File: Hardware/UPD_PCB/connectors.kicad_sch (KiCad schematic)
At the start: 26 parts, among them J1 25A Fuse holder, J10 796739-2, J11 Conn_01x02, J12 Conn_01x01, J2 796739-2, J3 Conn_01x02, J4 1776119-2, J5 1776119-2, J6 1776119-2, J7 1776119-2, J8 1776119-2, J9 1776119-2

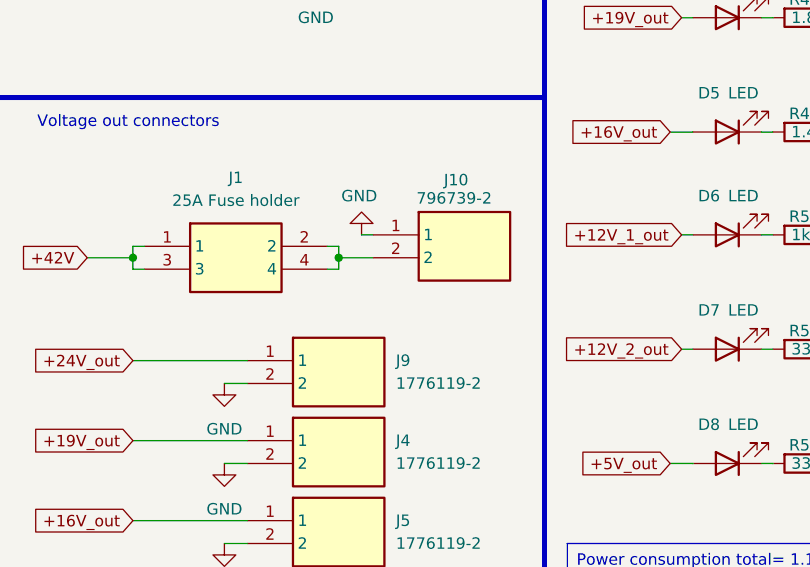
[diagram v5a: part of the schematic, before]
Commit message: Routed main traces
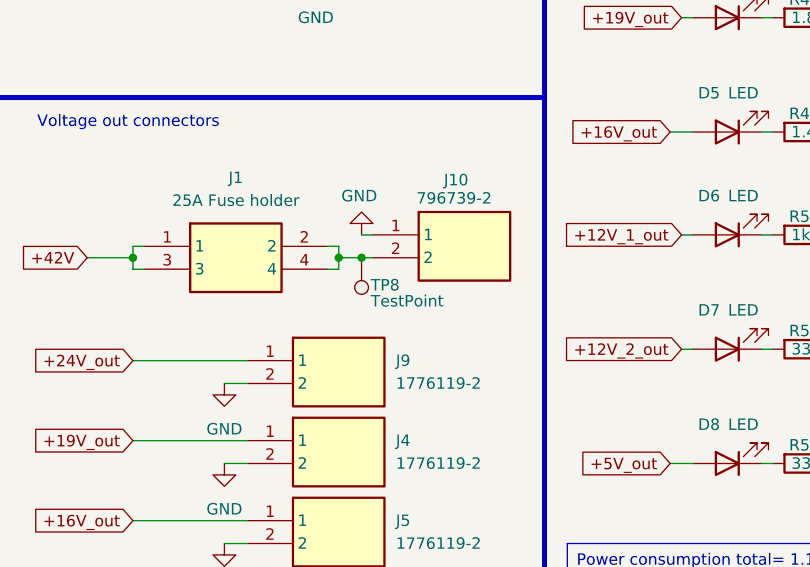
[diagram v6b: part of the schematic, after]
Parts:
- added TP8: TestPoint, TestPoint:TestPoint_THTPad_D1.0mm_Drill0.5mm, symbol Connector:TestPoint
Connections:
- net at J1.2, J1.4, J10.2: now also TP8.1
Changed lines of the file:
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@@
+	)
+	(junction
+		(at 68.58 87.63)
+		(diameter 0)
+		(color 0 0 0 0)
 	)
 	(junction
@@
 	(wire
 		(pts
-			(xy 66.04 87.63) (xy 69.85 87.63)
+			(xy 66.04 87.63) (xy 68.58 87.63)
 		)
 		(stroke
@@
 		(pts
 			(xy 113.03 60.96) (xy 114.3 60.96)
+		)
+		(stroke
+			(width 0)
+			(type default)
+		)
+	)
+	(wire
+		(pts
+			(xy 68.58 87.63) (xy 69.85 87.63)
 		)
 		(stroke
@@
 					(unit 1)
 				)
+			)
+		)
+	)
+	(symbol
+		(lib_id "Connector:TestPoint")
+		(at 68.58 87.63 180)
+		(unit 1)
+		(exclude_from_sim no)
+		(in_bom yes)
+		(on_board yes)
+		(dnp no)
+		(property "Reference" "TP8"
+			(at 69.596 90.678 0)
+			(effects
+				(font
+					(size 1.27 1.27)
+				)
+				(justify right)
+			)
+		)
+		(property "Value" "TestPoint"
+			(at 69.596 92.456 0)
+			(effects
+				(font
+					(size 1.27 1.27)
+				)
+				(justify right)
+			)
+		)
+		(property "Footprint" "TestPoint:TestPoint_THTPad_D1.0mm_Drill0.5mm"
+			(at 63.5 87.63 0)
+			(effects
+				(font
+					(size 1.27 1.27)
+				)
+				(hide yes)
+			)
+		)
+		(property "Datasheet" "~"
+			(at 63.5 87.63 0)
+			(effects
+				(font
+					(size 1.27 1.27)
+				)
+				(hide yes)
+			)
+		)
+		(property "Description" "test point"
+			(at 68.58 87.63 0)
+			(effects
+				(font
+					(size 1.27 1.27)
+				)
+				(hide yes)
+			)
+		)
+		(pin "1"
+		)
+		(instances
+			(project "UPD_PCB"
+				(path "/0650c7a8-acba-429c-9f8e-eec0baf0bc1c/fede4c36-00cc-4d3d-b71c-5243ba232202/7d5a1283-086b-46b0-8df7-a9850521fb5e/4a3b49c6-ce69-4997-95b2-b7bb4e96c397"
+					(reference "TP8")
+					(unit 1)
+				)

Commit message: Final pcb before review
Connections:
- net +42V: no longer D2.2 (A)
- net +42V_out: now reaches J1.2, J1.4, J10.2, TP8.1
- net +42V_out: now also D2.2 (A)
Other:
- moved on the sheet: J10
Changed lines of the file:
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@@
 	(wire
 		(pts
-			(xy 68.58 85.09) (xy 69.85 85.09)
+			(xy 68.58 85.09) (xy 73.66 85.09)
 		)
 		(stroke
@@
 	(wire
 		(pts
+			(xy 113.03 48.26) (xy 114.3 48.26)
+		)
+		(stroke
+			(width 0)
+			(type default)
+		)
+	)
+	(wire
+		(pts
+			(xy 43.18 86.36) (xy 44.45 86.36)
+		)
+		(stroke
+			(width 0)
+			(type default)
+		)
+	)
+	(wire
+		(pts
+			(xy 104.14 48.26) (xy 105.41 48.26)
+		)
+		(stroke
+			(width 0)
+			(type default)
+		)
+	)
+	(wire
+		(pts
+			(xy 121.92 60.96) (xy 121.92 62.23)
+		)
+		(stroke
+			(width 0)
+			(type default)
+		)
+	)
+	(wire
+		(pts
+			(xy 113.03 110.49) (xy 114.3 110.49)
+		)
+		(stroke
+			(width 0)
+			(type default)
+		)
+	)
+	(wire
+		(pts
+			(xy 43.18 99.06) (xy 55.88 99.06)
+		)
+		(stroke
+			(width 0)
+			(type default)
+		)
+	)
+	(wire
+		(pts
+			(xy 104.14 97.79) (xy 105.41 97.79)
+		)
+		(stroke
+			(width 0)
+			(type default)
+		)
+	)
+	(wire
+		(pts
+			(xy 53.34 119.38) (xy 55.88 119.38)
+		)
+		(stroke
+			(width 0)
+			(type default)
+		)
+	)
+	(wire
+		(pts
+			(xy 53.34 128.27) (xy 55.88 128.27)
+		)
+		(stroke
+			(width 0)
+			(type default)
+		)
+	)
+	(wire
+		(pts
+			(xy 43.18 87.63) (xy 43.18 86.36)
+		)
+		(stroke
+			(width 0)
+			(type default)
+		)
+	)
+	(wire
+		(pts
+			(xy 53.34 101.6) (xy 55.88 101.6)
+		)
+		(stroke
+			(width 0)
+			(type default)
+		)
+	)
+	(wire
+		(pts
+			(xy 113.03 60.96) (xy 114.3 60.96)
+		)
+		(stroke
+			(width 0)
+			(type default)
+		)
+	)
+	(wire
+		(pts
+			(xy 68.58 87.63) (xy 73.66 87.63)
+		)
+		(stroke
+			(width 0)
+			(type default)
+		)
+	)
+	(wire
+		(pts
+			(xy 38.1 87.63) (xy 43.18 87.63)
+		)
+		(stroke
+			(width 0)
+			(type default)
+		)
+	)
+	(wire
+		(pts
 			(xy 66.04 87.63) (xy 68.58 87.63)
 		)
@@
 	(wire
 		(pts
-			(xy 113.03 48.26) (xy 114.3 48.26)
-		)
-		(stroke
-			(width 0)
-			(type default)
-		)
-	)
-	(wire
-		(pts
-			(xy 43.18 86.36) (xy 44.45 86.36)
-		)
-		(stroke
-			(width 0)
-			(type default)
-		)
-	)
-	(wire
-		(pts
-			(xy 104.14 48.26) (xy 105.41 48.26)
-		)
-		(stroke
-			(width 0)
-			(type default)
-		)
-	)
-	(wire
-		(pts
-			(xy 121.92 60.96) (xy 121.92 62.23)
-		)
-		(stroke
-			(width 0)
-			(type default)
-		)
-	)
-	(wire
-		(pts
-			(xy 113.03 110.49) (xy 114.3 110.49)
-		)
-		(stroke
-			(width 0)
-			(type default)
-		)
-	)
-	(wire
-		(pts
-			(xy 43.18 99.06) (xy 55.88 99.06)
-		)
-		(stroke
-			(width 0)
-			(type default)
-		)
-	)
-	(wire
-		(pts
-			(xy 104.14 97.79) (xy 105.41 97.79)
-		)
-		(stroke
-			(width 0)
-			(type default)
-		)
-	)
-	(wire
-		(pts
-			(xy 53.34 119.38) (xy 55.88 119.38)
-		)
-		(stroke
-			(width 0)
-			(type default)
-		)
-	)
-	(wire
-		(pts
-			(xy 53.34 128.27) (xy 55.88 128.27)
-		)
-		(stroke
-			(width 0)
-			(type default)
-		)
-	)
-	(wire
-		(pts
-			(xy 43.18 87.63) (xy 43.18 86.36)
-		)
-		(stroke
-			(width 0)
-			(type default)
-		)
-	)
-	(wire
-		(pts
-			(xy 53.34 101.6) (xy 55.88 101.6)
-		)
-		(stroke
-			(width 0)
-			(type default)
-		)
-	)
-	(wire
-		(pts
-			(xy 113.03 60.96) (xy 114.3 60.96)
-		)
-		(stroke
-			(width 0)
-			(type default)
-		)
-	)
-	(wire
-		(pts
-			(xy 68.58 87.63) (xy 69.85 87.63)
-		)
-		(stroke
-			(width 0)
-			(type default)
-		)
-	)
-	(wire
-		(pts
-			(xy 38.1 87.63) (xy 43.18 87.63)
-		)
-		(stroke
-			(width 0)
-			(type default)
-		)
-	)
-	(wire
-		(pts
 			(xy 121.92 36.83) (xy 121.92 38.1)
 		)
@@
 	(wire
 		(pts
-			(xy 100.33 36.83) (xy 105.41 36.83)
+			(xy 104.14 36.83) (xy 105.41 36.83)
 		)
 		(stroke
@@
 		)
 	)
+	(label "+42V_out"
+		(at 66.04 87.63 0)
+		(fields_autoplaced yes)
+		(effects
+			(font
+				(size 1.27 1.27)
+			)
+			(justify left bottom)
+		)
+	)
 	(global_label "INA_SCL"
 		(shape input)
@@
 		)
 	)
-	(global_label "+42V"
+	(global_label "+42V_out"
 		(shape input)
-		(at 100.33 36.83 180)
+		(at 104.14 36.83 180)
 		(fields_autoplaced yes)
 		(effects
@@
 		)
 		(property "Intersheetrefs" "${INTERSHEET_REFS}"
-			(at 92.2648 36.83 0)
+			(at 92.0835 36.83 0)
 			(effects
 				(font
@@
 	(symbol
 		(lib_id "796739-2:796739-2")
-		(at 69.85 85.09 0)
+		(at 73.66 85.09 0)
 		(unit 1)
 		(exclude_from_sim no)
@@
 		(dnp no)
 		(property "Reference" "J10"
-			(at 77.724 78.994 0)
+			(at 81.534 78.994 0)
 			(effects
 				(font
@@
 		)
 		(property "Value" "796739-2"
-			(at 74.676 81.026 0)
+			(at 78.486 81.026 0)
 			(effects
 				(font
@@
 		)
 		(property "Footprint" "7967392"
-			(at 86.36 180.01 0)
+			(at 90.17 180.01 0)
 			(effects
 				(font
@@
 		)
 		(property "Datasheet" "https://www.te.com/commerce/DocumentDelivery/DDEController?Action=srchrtrv&DocNm=1-1773458-1_EURO_STYLE_QRG&DocType=Data%20Sheet&DocLang=English&PartCntxt=796739-2&DocFormat=pdf"
-			(at 86.36 280.01 0)
+			(at 90.17 280.01 0)
 			(effects
 				(font
@@
 		)
 		(property "Description" "Body Features: Product Orientation Vertical | Primary Product Color Green | Configuration Features: Wire Entry Angle 90 | Stacked Levels Without | Number of Positions 2 | Number of Rows 1 | Wire Entry Location Side | Contact Features: Contact Base Material Brass | Contact Current Rating (Max) 30 AMP | Contact Mating Area Plating Material Tin | Dimensions: Wire Size .05  5.26 MMSQ | Wire Size 30  10 AWG | Electrical Characteristics: Operating Voltage 600 VAC | Housing Features: Housing Material PA 66"
-			(at 69.85 85.09 0)
+			(at 73.66 85.09 0)
 			(effects
 				(font
@@
 		)
 		(property "Height" "21.7"
-			(at 86.36 480.01 0)
+			(at 90.17 480.01 0)
 			(effects
 				(font
@@
 		)
 		(property "Mouser Part Number" "571-796739-2"
-			(at 86.36 580.01 0)
+			(at 90.17 580.01 0)
 			(effects
 				(font
@@
 		)
 		(property "Mouser Price/Stock" "https://www.mouser.co.uk/ProductDetail/TE-Connectivity/796739-2?qs=DUs9f6OUnucjHXAXMBymqQ%3D%3D"
-			(at 86.36 680.01 0)
+			(at 90.17 680.01 0)
 			(effects
 				(font
@@
 		)
 		(property "Manufacturer_Name" "TE Connectivity"
-			(at 86.36 780.01 0)
+			(at 90.17 780.01 0)
 			(effects
 				(font
@@
 		)
 		(property "Manufacturer_Part_Number" "796739-2"
-			(at 86.36 880.01 0)
-			(effects
-				(font
+			(at 90.17 880.01 0)
+			(effects
+				(font

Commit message: Finalized PCB
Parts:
- removed J11: Conn_01x02, Connector_PinHeader_1.00mm:PinHeader_1x02_P1.00mm_Vertical, symbol Connector_Generic:Conn_01x02
- removed J12: Conn_01x01, Connector_PinHeader_1.00mm:PinHeader_1x01_P1.00mm_Vertical, symbol Connector_Generic:Conn_01x01
- added J11: Conn_01x04, Connector:NS-Tech_Grove_1x04_P2mm_Vertical, symbol Connector_Generic:Conn_01x04
- added J12: Conn_01x02, Connector_PinHeader_1.00mm:PinHeader_1x02_P1.00mm_Vertical, symbol Connector_Generic:Conn_01x02
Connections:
- net +5V_out: now also J11.2 (Pin_2)
- net GND: now also J11.1 (Pin_1), J12.1 (Pin_1)
- net INA_SCL: now also J11.4 (Pin_4)
- net INA_SDA: now also J11.3 (Pin_3)
- net VIOUT: now also J12.2 (Pin_2)
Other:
- moved on the sheet: J10
